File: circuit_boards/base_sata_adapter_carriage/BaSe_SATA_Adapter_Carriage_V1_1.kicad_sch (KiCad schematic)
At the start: 7 parts

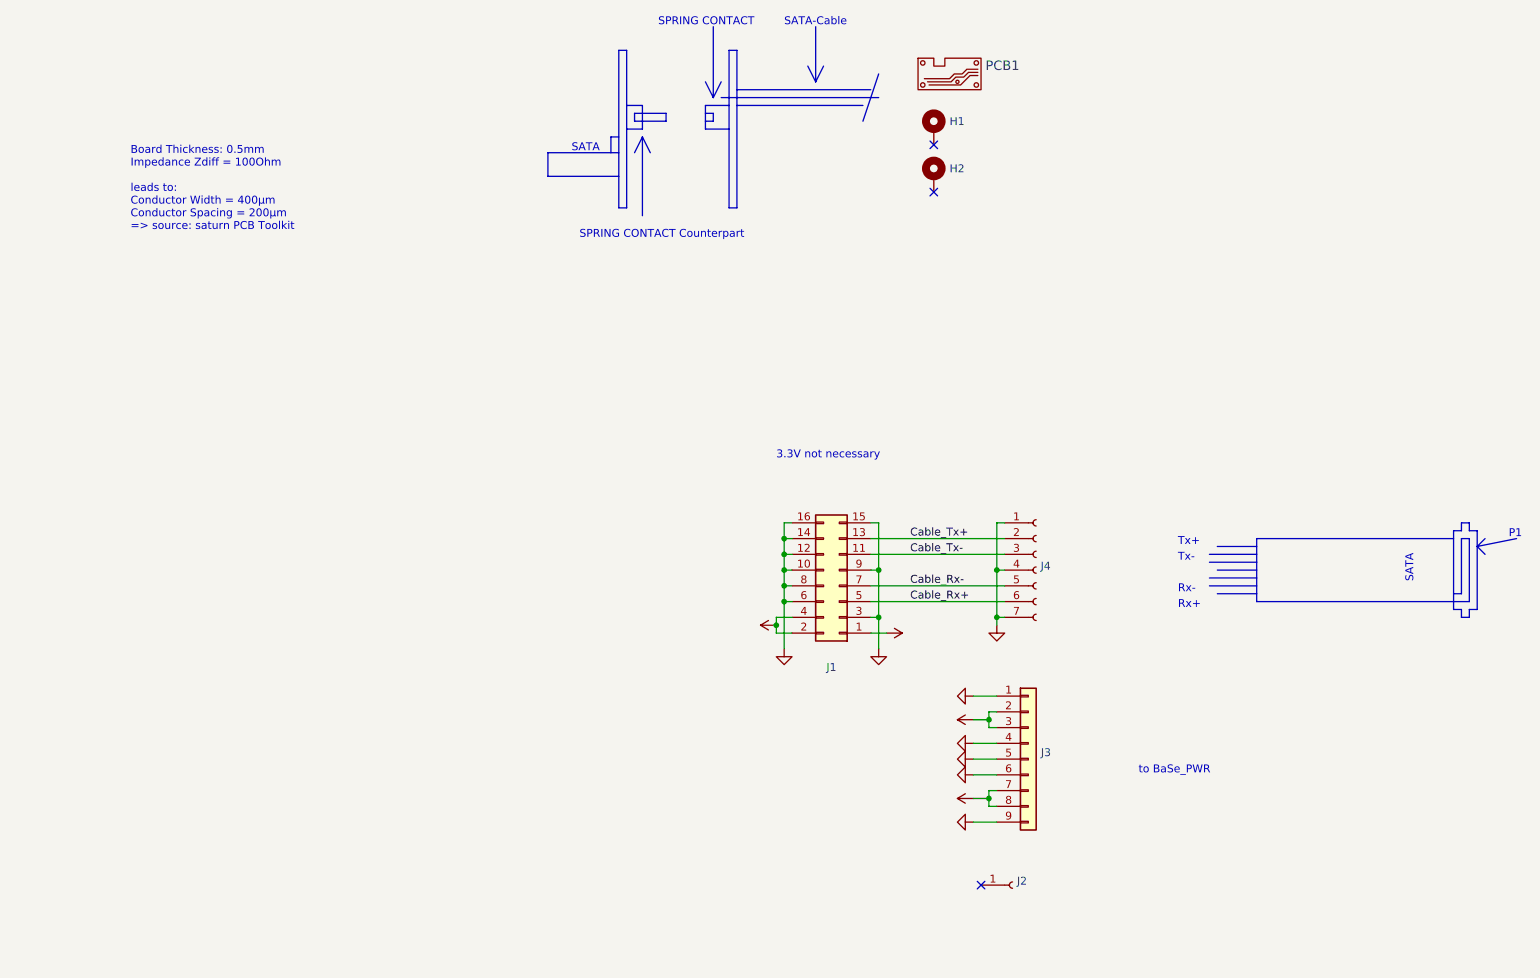
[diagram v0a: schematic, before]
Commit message: [HW] production ready versions of sata adapter boards
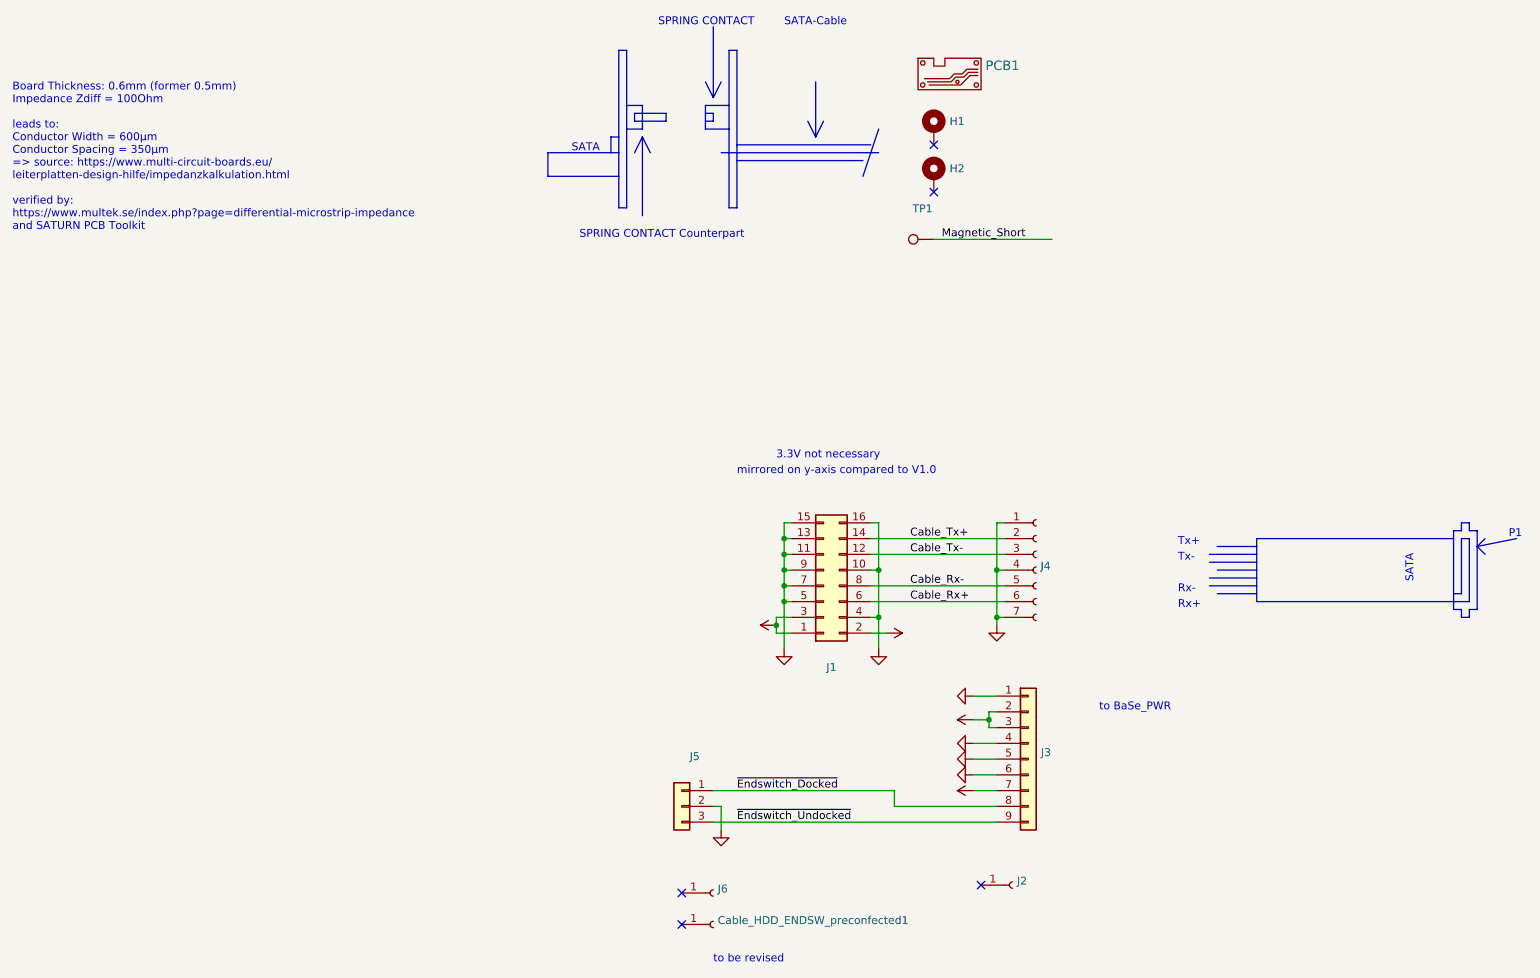
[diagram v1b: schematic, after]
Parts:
- added Cable_HDD_ENDSW_preconfected1, J6: (no value), symbol Connector:Conn_01x01_Female
- added J5: (no value), symbol Connector_Generic:Conn_01x03
- added TP1: (no value), symbol Connector:TestPoint
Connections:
- net +12VA: now also J1.1 (Pin_1), J1.3 (Pin_3); no longer J1.2 (Pin_2), J1.4 (Pin_4)
- net +5VA: now also J1.2 (Pin_2); no longer J1.1 (Pin_1), J3.8 (Pin_8)
- net Cable_Rx+: now also J1.6 (Pin_6); no longer J1.5 (Pin_5)
- net Cable_Rx-: now also J1.8 (Pin_8); no longer J1.7 (Pin_7)
- net Cable_Tx+: now also J1.14 (Pin_14); no longer J1.13 (Pin_13)
- net Cable_Tx-: now also J1.12 (Pin_12); no longer J1.11 (Pin_11)
- net GNDA: now also J1.11 (Pin_11), J1.13 (Pin_13), J1.4 (Pin_4), J1.5 (Pin_5), J1.7 (Pin_7), J5.2 (Pin_2); no longer J1.12 (Pin_12), J1.14 (Pin_14), J1.3 (Pin_3), J1.6 (Pin_6), J1.8 (Pin_8), J3.9 (Pin_9)
- new net Magnetic_Short: TP1.1
- new net ~{Endswitch_Docked}: J3.8 (Pin_8), J5.1 (Pin_1)
- new net ~{Endswitch_Undocked}: J3.9 (Pin_9), J5.3 (Pin_3)
- no-connect marks 3 -> 5
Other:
- note added: "Board Thickness: 0.6mm (former 0.5mm) Impedance Zdiff = 100Ohm leads to: Conductor Width = 600µm Conductor Spacing = 350µm => source: https://www.multi-circuit-boards.eu/ leiterplatten-design-hilfe/impedanzkalkulation.html verified by: https://www.multek.se/index.php?page=differential-microstrip-impedance and SATURN PCB Toolkit"
- note added: "mirrored on y-axis compared to V1.0"
- note added: "to be revised"
- note removed: "Board Thickness: 0.5mm Impedance Zdiff = 100Ohm leads to: Conductor Width = 400µm Conductor Spacing = 200µm => source: saturn PCB Toolkit"
- title: BaSe_SATA_Adapter_Carriage_V1_0 -> BaSe_SATA_Adapter_Carriage_V1_1
- moved on the sheet: J1
